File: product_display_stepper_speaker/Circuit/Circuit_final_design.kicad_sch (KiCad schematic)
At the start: 18 parts, among them J1 Barrel_Jack_MountingPin, U1 ESP-12E, U2 LM2931-3.3_TO220, U3 L7805

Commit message: finished pcb layout
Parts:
- removed U1: ESP-12E, ESP:ESP-12E-DIP, symbol RF_Module:ESP-12E
- removed U3: L7805, Package_TO_SOT_THT:TO-220-3_Vertical, symbol Regulator_Linear:L7805
- added Bridge1: 0, Resistor_THT:R_Axial_DIN0207_L6.3mm_D2.5mm_P7.62mm_Horizontal, symbol Device:R
- added U1: L7805, Package_TO_SOT_THT:TO-220-3_Vertical, symbol Regulator_Linear:L7805
- added U3: ESP-12E, ESP:ESP-12E-DIP, symbol RF_Module:ESP-12E
- C1: value 470uf -> 330uf
- C2: value 330uf -> 470uf
- R1: footprint Resistor_THT:R_Axial_DIN0207_L6.3mm_D2.5mm_P7.62mm_Horizontal -> Resistor_THT:R_Axial_DIN0207_L6.3mm_D2.5mm_P5.08mm_Vertical
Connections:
- net +12V: now also C2.1, U1.1 (IN); no longer C1.1
- net +3.3V: now also C1.1, U3.8 (VCC); no longer C2.1
- net +5V: now also U1.3 (OUT)
- net DIR1: now also A2.16 (DIR), U3.6 (GPIO12); no longer A1.16 (DIR)
- net DIR2: now also A1.16 (DIR), U3.4 (GPIO16); no longer A2.16 (DIR)
- net EN: now also Bridge1.1, U3.16 (GPIO15); no longer A1.9 (~{EN})
- net GND: now also U1.2 (GND), U3.15 (GND), U3.17 (GPIO2)
- net RX: now also U3.21 (GPIO3/RXD)
- net Reset: now also U3.3 (EN)
- net STEP1: now also A2.15 (STEP), U3.7 (GPIO13); no longer A1.15 (STEP)
- net STEP2: now also A1.15 (STEP), U3.5 (GPIO14); no longer A2.15 (STEP)
- net TX: now also U3.22 (GPIO1/TXD)
- net mode: now also U3.18 (GPIO0)
- net speaker_l: now also U3.19 (GPIO4)
- net speaker_r: now also U3.20 (GPIO5)
- new net: A1.9 (~{EN}), Bridge1.2

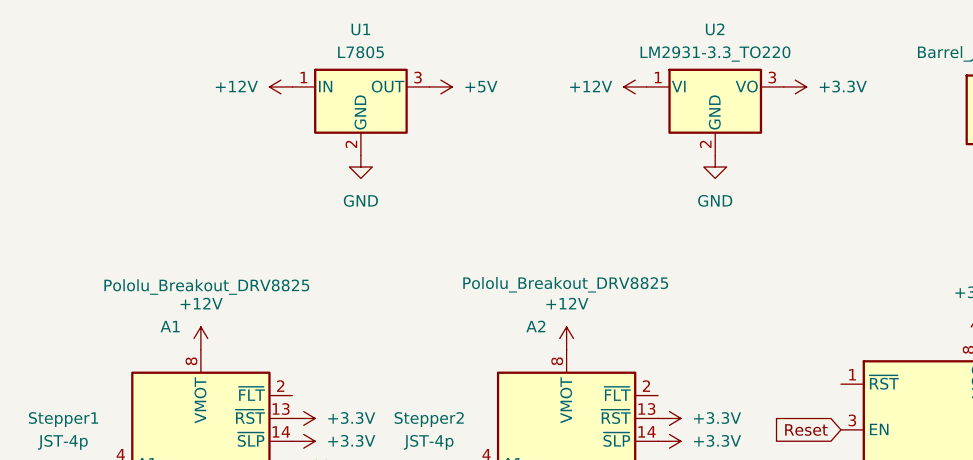
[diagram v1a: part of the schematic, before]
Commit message: finished circuits of both hospital rover and product display with speakers and steppers projects
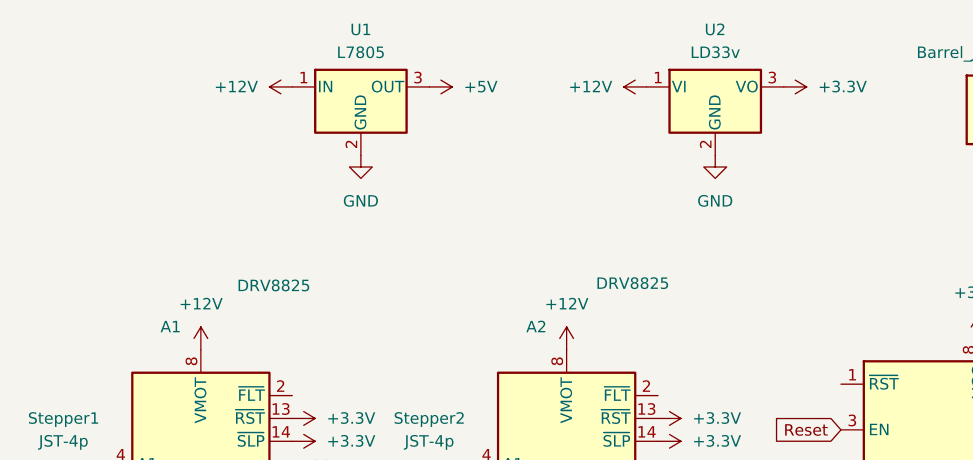
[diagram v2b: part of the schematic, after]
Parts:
- A1, A2: value Pololu_Breakout_DRV8825 -> DRV8825
- U2: value LM2931-3.3_TO220 -> LD33v
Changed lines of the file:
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@@
 			)
 		)
-		(property "Value" "Pololu_Breakout_DRV8825"
+		(property "Value" "DRV8825"
 			(at 94.742 80.518 0)
 			(effects
@@
 			)
 		)
-		(property "Value" "Pololu_Breakout_DRV8825"
+		(property "Value" "DRV8825"
 			(at 134.62 80.264 0)
 			(effects
@@
 			)
 		)
-		(property "Value" "LM2931-3.3_TO220"
+		(property "Value" "LD33v"
 			(at 139.7 54.61 0)
 			(effects

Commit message: major circuit fixing for both current projects
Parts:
- removed U2: LD33v, Package_TO_SOT_THT:TO-220-3_Vertical, symbol Regulator_Linear:LM2931-3.3_TO220
- added R3: 10k, Resistor_THT:R_Axial_DIN0207_L6.3mm_D2.5mm_P7.62mm_Horizontal, symbol Device:R
- added U2: LD33v, Package_TO_SOT_THT:TO-220-3_Vertical, symbol ld33v:LD33v
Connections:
- net +12V: now also U2.3 (Vin)
- net +3.3V: now also R3.1, U2.2 (Vout)
- net GND: now also U2.1 (GND); no longer U3.17 (GPIO2)
- new net: R3.2, U3.17 (GPIO2)
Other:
- moved on the sheet: Debug1

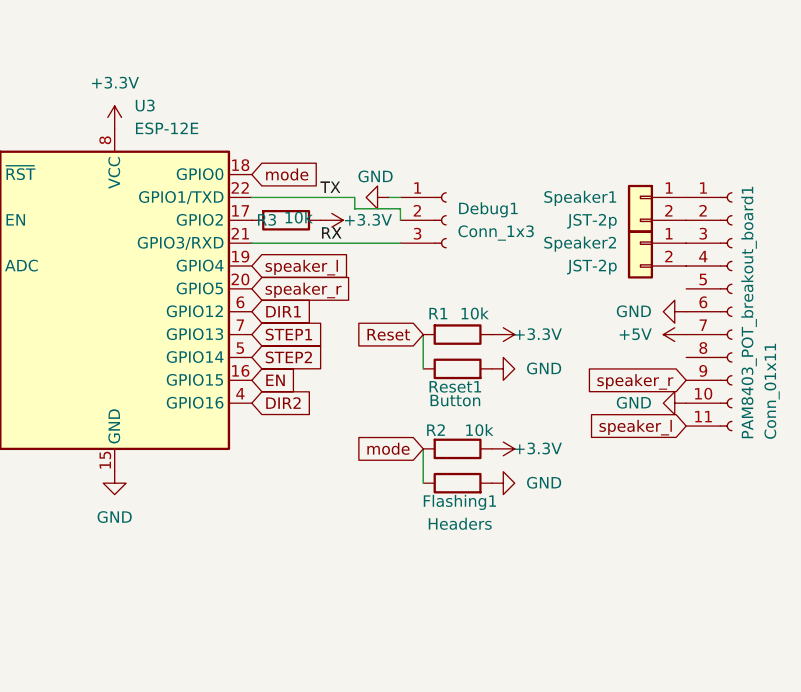
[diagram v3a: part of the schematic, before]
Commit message: started programming product display stepper speaker project
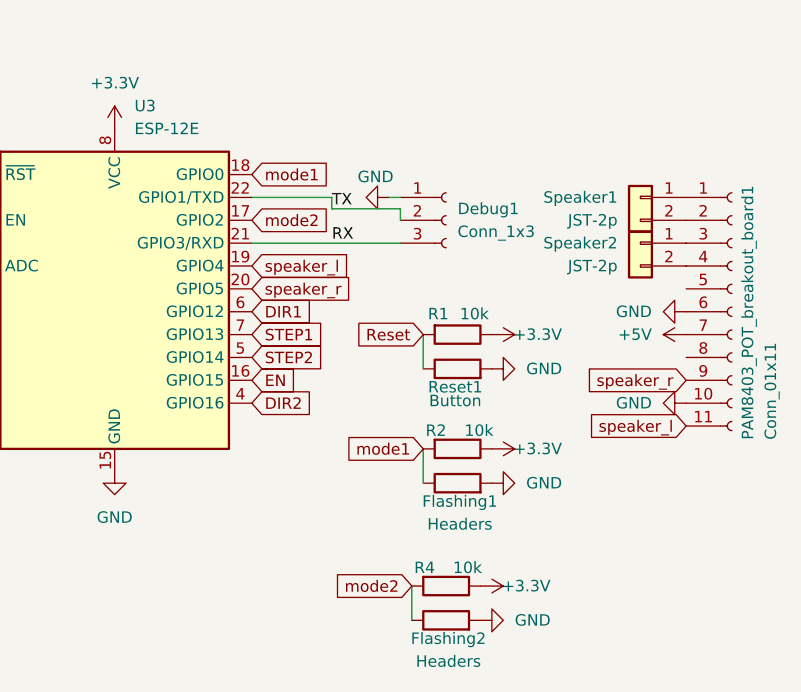
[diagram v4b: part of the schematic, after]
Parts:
- removed R3: 10k, Resistor_THT:R_Axial_DIN0207_L6.3mm_D2.5mm_P7.62mm_Horizontal, symbol Device:R
- added Flashing2: Headers, Resistor_THT:R_Axial_DIN0207_L6.3mm_D2.5mm_P2.54mm_Vertical, symbol Device:R
- added R4: 10k, Resistor_THT:R_Axial_DIN0207_L6.3mm_D2.5mm_P7.62mm_Horizontal, symbol Device:R
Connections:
- net +3.3V: now also R4.1
- net GND: now also Flashing2.2
- net mode2: now reaches U3.17 (GPIO2)
- net mode2: now also Flashing2.1, R4.2
- net mode renamed mode1

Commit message: added circuit step files for both current projects
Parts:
- A1, A2: footprint Module:Pololu_Breakout-16_15.2x20.3mm -> DRV8825:DRV8825_module
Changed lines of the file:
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@@
 			)
 		)
-		(property "Footprint" "Module:Pololu_Breakout-16_15.2x20.3mm"
+		(property "Footprint" "DRV8825:DRV8825_module"
 			(at 77.47 123.19 0)
 			(effects
@@
 			)
 		)
-		(property "Footprint" "Module:Pololu_Breakout-16_15.2x20.3mm"
+		(property "Footprint" "DRV8825:DRV8825_module"
 			(at 118.11 123.19 0)
 			(effects
